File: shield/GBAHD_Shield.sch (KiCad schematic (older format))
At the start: 17 parts, among them J1 Conn_01x40, J2 Conn_02x08_Top_Bottom, J3 Conn_01x16, J4 Conn_02x10_Top_Bottom, J5 Conn_01x05, J6 Conn_02x03_Odd_Even, J7 Conn_01x01, SW1 SW_Push, U1 SNES_7PIN, U2 ATmega328P-AU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

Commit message: Version 2 initial commit.
- Changed board layout
- Changed breakout board pin order
- Changed FFC connectors
- Added connectors for 32 pin and 34 pin
- Changed SNES connector to Classic connector.
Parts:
- removed J5: Conn_01x05, OFFSET:Pads_01x05, symbol Connector_Generic:Conn_01x05
- removed J7: Conn_01x01, OFFSET:SOLDER_PAD, symbol Connector_Generic:Conn_01x01
- removed SJ1: SOLDER_JUMPER, Jumper:SolderJumper-2_P1.3mm_Open_RoundedPad1.0x1.5mm, symbol keyboard_parts:SOLDER_JUMPER
- removed U1: SNES_7PIN, OFFSET:SNES_7PIN, symbol Raizu:SNES_7PIN
- removed U3: WAS3157B, OFFSET:SOT-363, symbol Raizu:WAS3157B
- added J5: Conn_01x34, Raizu:JUSHUO_AFC07-S34FCC-00, symbol Connector_Generic:Conn_01x34
- added J7: Conn_01x32, Raizu:JUSHUO_AFC01-S32FCC-00, symbol Connector_Generic:Conn_01x32
- added P1: CONN_WII, Raizu_OFFSET:CONN_WII, symbol Raizu:CONN_WII
- added TP1: EX1, Raizu_OFFSET:SOLDER_PAD, symbol Connector:TestPoint
- added TP2: EX2, Raizu_OFFSET:SOLDER_PAD, symbol Connector:TestPoint
- added TP3: EX3, Raizu_OFFSET:SOLDER_PAD, symbol Connector:TestPoint
- added TP4: EX4, Raizu_OFFSET:SOLDER_PAD, symbol Connector:TestPoint
- J1: footprint OFFSET:JUSHUO_AFC07-S40FCC-00 -> Raizu:JUSHUO_AFC01-S40FCC-00
- J3: value Conn_01x16 -> Conn_01x20; footprint OFFSET:JUSHUO_AFC07-S16FCC-00 -> Raizu:JUSHUO_AFC01-S20FCC-00; symbol Connector_Generic:Conn_01x16 -> Connector_Generic:Conn_01x20
- SW1: footprint OFFSET:XKB-TS-1185EC-C-D-B -> Raizu_OFFSET:XKB-TS-1185EC-C-D-B
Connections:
- net labels added: GBA_RESET, JOY_DET, JOY_SCL, JOY_SDA
- net labels removed: GBA_POWER_SEL, SNS_CLK, SNS_DATA, SNS_LATCH
- wire segments 49 -> 59
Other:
- moved on the sheet: J2, J4

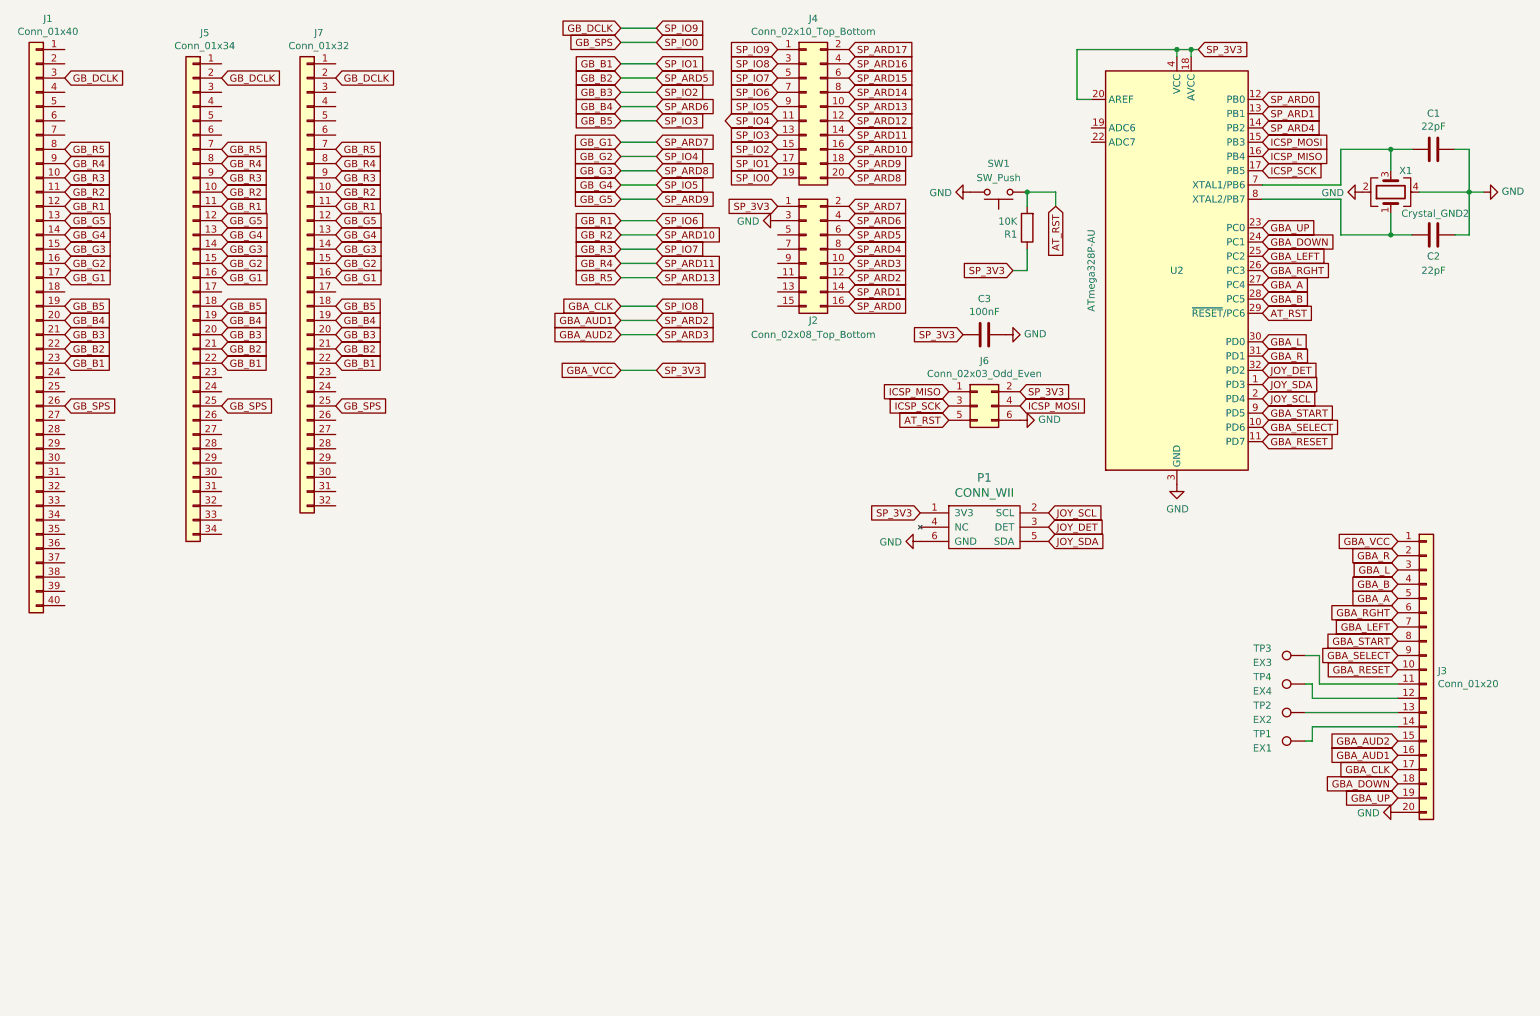
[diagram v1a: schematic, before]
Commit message: PCB changes and breakout board
- Added breakout to main board as a breakaway board.
- Added controller connector expansion for port relocation
- Tidying routing and other minimal changes
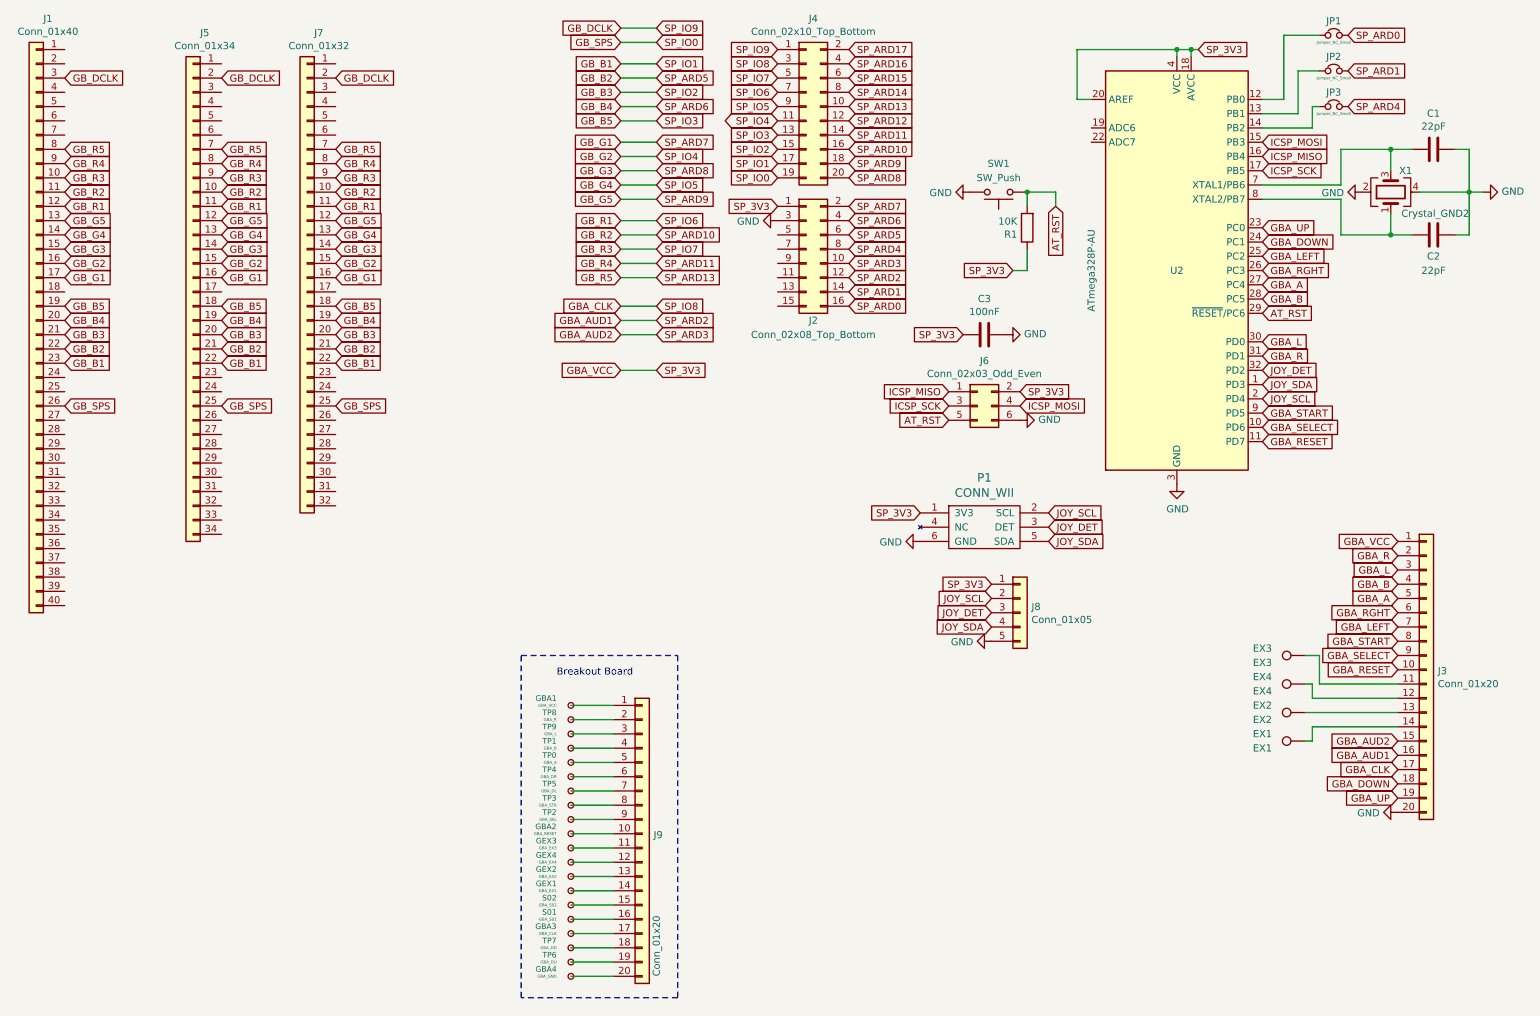
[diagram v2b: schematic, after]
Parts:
- added GBA1: GBA_VCC, Raizu_OFFSET:SOLDER_PAD, symbol Connector:TestPoint_Small
- added GBA2: GBA_RESET, Raizu_OFFSET:SOLDER_PAD, symbol Connector:TestPoint_Small
- added GBA3: GBA_CLK, Raizu_OFFSET:SOLDER_PAD, symbol Connector:TestPoint_Small
- added GBA4: GBA_GND, Raizu_OFFSET:SOLDER_PAD, symbol Connector:TestPoint_Small
- added GEX1: GBA_EX1, Raizu_OFFSET:SOLDER_PAD, symbol Connector:TestPoint_Small
- added GEX2: GBA_EX2, Raizu_OFFSET:SOLDER_PAD, symbol Connector:TestPoint_Small
- added GEX3: GBA_EX3, Raizu_OFFSET:SOLDER_PAD, symbol Connector:TestPoint_Small
- added GEX4: GBA_EX4, Raizu_OFFSET:SOLDER_PAD, symbol Connector:TestPoint_Small
- added J8: Conn_01x05, Connector_PinHeader_2.54mm:PinHeader_1x05_P2.54mm_Horizontal, symbol Connector_Generic:Conn_01x05
- added J9: Conn_01x20, Raizu:JUSHUO_AFC01-S20FCC-00, symbol Connector_Generic:Conn_01x20
- added JP1, JP2, JP3: Jumper_NC_Small, Jumper:SolderJumper-2_P1.3mm_Bridged_RoundedPad1.0x1.5mm, symbol Device:Jumper_NC_Small
- added S01: GBA_S01, Raizu_OFFSET:SOLDER_PAD, symbol Connector:TestPoint_Small
- added S02: GBA_S02, Raizu_OFFSET:SOLDER_PAD, symbol Connector:TestPoint_Small
- added TP0: GBA_A, Raizu_OFFSET:SOLDER_PAD, symbol Connector:TestPoint_Small
- added TP1: GBA_B, Raizu_OFFSET:SOLDER_PAD, symbol Connector:TestPoint_Small
- added TP2: GBA_SEL, Raizu_OFFSET:SOLDER_PAD, symbol Connector:TestPoint_Small
- added TP3: GBA_STR, Raizu_OFFSET:SOLDER_PAD, symbol Connector:TestPoint_Small
- added TP4: GBA_DR, Raizu_OFFSET:SOLDER_PAD, symbol Connector:TestPoint_Small
- added TP5: GBA_DL, Raizu_OFFSET:SOLDER_PAD, symbol Connector:TestPoint_Small
- added TP6: GBA_DU, Raizu_OFFSET:SOLDER_PAD, symbol Connector:TestPoint_Small
- added TP7: GBA_DD, Raizu_OFFSET:SOLDER_PAD, symbol Connector:TestPoint_Small
- added TP8: GBA_R, Raizu_OFFSET:SOLDER_PAD, symbol Connector:TestPoint_Small
- added TP9: GBA_L, Raizu_OFFSET:SOLDER_PAD, symbol Connector:TestPoint_Small
- renumbered TP1 to EX1, TP2 to EX2, TP3 to EX3, TP4 to EX4
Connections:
- net GBA_VCC: now also J8.1 (Pin_1)
- net GND: now also J8.5 (Pin_5)
- net JOY_DET: now also J8.3 (Pin_3)
- net JOY_SCL: now also J8.2 (Pin_2)
- net JOY_SDA: now also J8.4 (Pin_4)
- net SP_ARD0: now also JP1.2; no longer U2.12 (PB0)
- net SP_ARD1: now also JP2.2; no longer U2.13 (PB1)
- net SP_ARD4: now also JP3.2; no longer U2.14 (PB2)
- new net: JP1.1, U2.12 (PB0)
- new net: JP2.1, U2.13 (PB1)
- new net: JP3.1, U2.14 (PB2)
- new net: GBA1.1, J9.1 (Pin_1)
- new net: GBA2.1, J9.10 (Pin_10)
- new net: GEX3.1, J9.11 (Pin_11)
- new net: GEX4.1, J9.12 (Pin_12)
- new net: GEX2.1, J9.13 (Pin_13)
- new net: GEX1.1, J9.14 (Pin_14)
- new net: J9.15 (Pin_15), S02.1
- new net: J9.16 (Pin_16), S01.1
- new net: GBA3.1, J9.17 (Pin_17)
- new net: J9.18 (Pin_18), TP7.1
- new net: J9.19 (Pin_19), TP6.1
- new net: J9.2 (Pin_2), TP8.1
- new net: GBA4.1, J9.20 (Pin_20)
- new net: J9.3 (Pin_3), TP9.1
- new net: J9.4 (Pin_4), TP1.1
- new net: J9.5 (Pin_5), TP0.1
- new net: J9.6 (Pin_6), TP4.1
- new net: J9.7 (Pin_7), TP5.1
- new net: J9.8 (Pin_8), TP3.1
- new net: J9.9 (Pin_9), TP2.1
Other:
- note added: "Breakout Board"

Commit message: PCB design work
- Added extension board (controller, LED and power switch)
- Panelized board
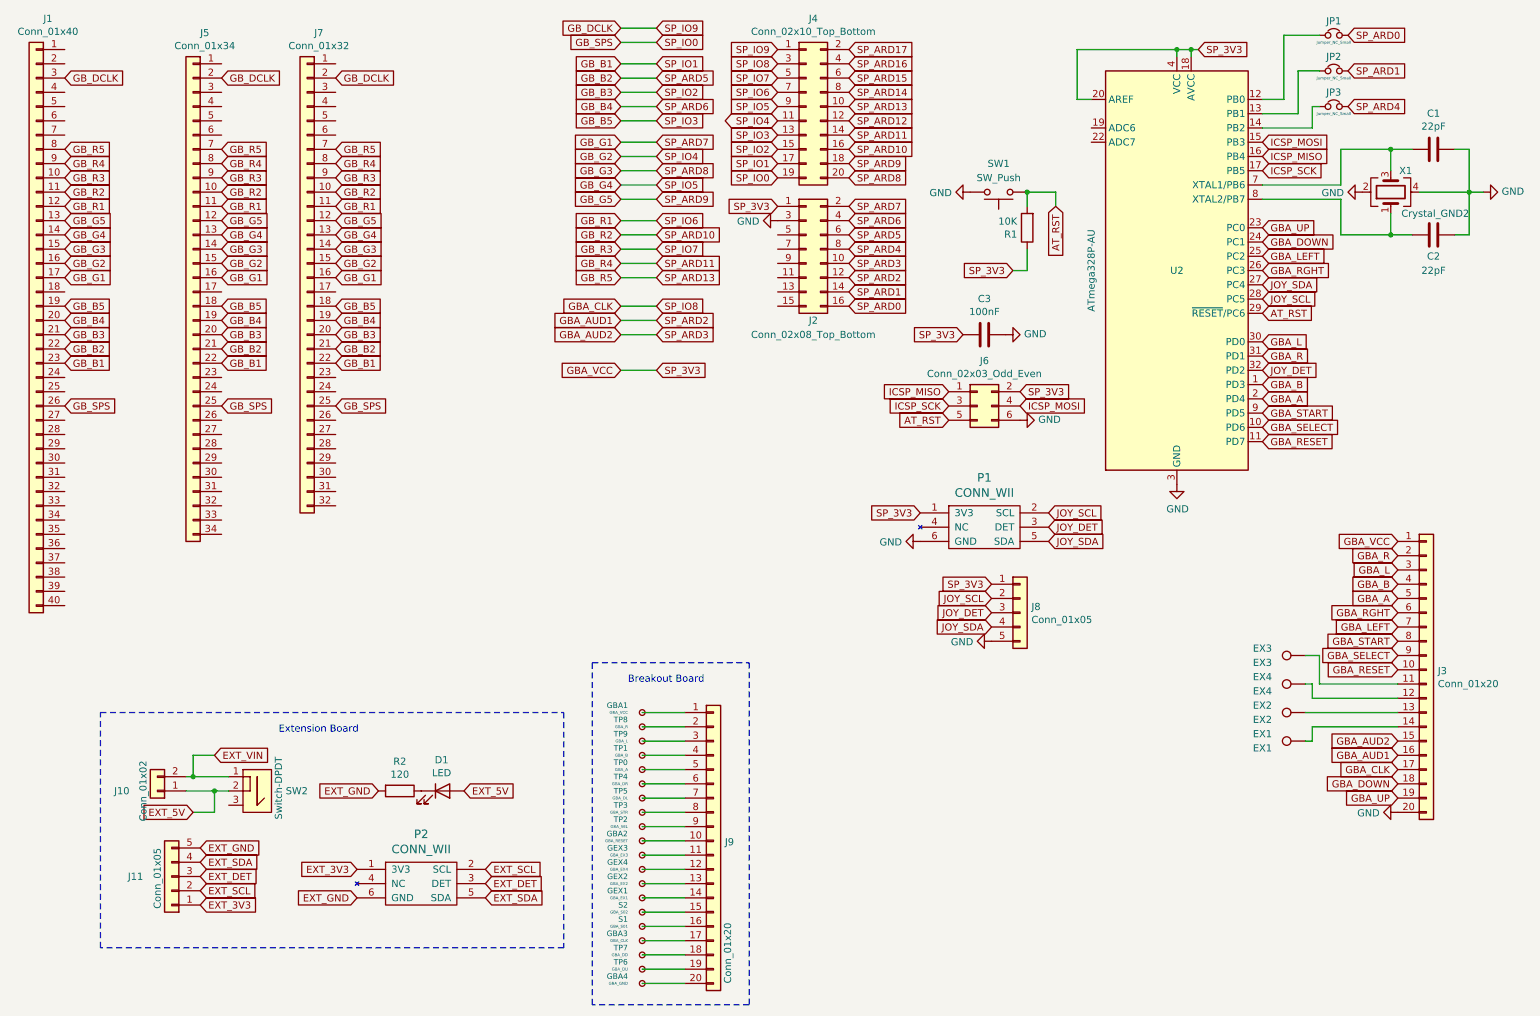
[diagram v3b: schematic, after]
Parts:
- added D1: LED, LED_THT:LED_D5.0mm_FlatTop, symbol Device:LED
- added J10: Conn_01x02, Connector_PinHeader_2.54mm:PinHeader_1x02_P2.54mm_Horizontal, symbol Connector_Generic:Conn_01x02
- added J11: Conn_01x05, Connector_PinHeader_2.54mm:PinHeader_1x05_P2.54mm_Horizontal, symbol Connector_Generic:Conn_01x05
- added P2: CONN_WII, Raizu_OFFSET:CONN_WII, symbol Raizu:CONN_WII
- added R2: 120, Resistor_SMD:R_0805_2012Metric_Pad1.20x1.40mm_HandSolder, symbol Device:R
- added SW2: Switch-DPDT, Raizu_OFFSET:XKB_XKB5858-Z-C, symbol Raizu:Switch-DPDT
- renumbered S01 to S1, S02 to S2
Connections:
- net GBA_A: now also U2.2 (PD4); no longer U2.27 (PC4)
- net GBA_B: now also U2.1 (PD3); no longer U2.28 (PC5)
- net JOY_SCL: now also U2.28 (PC5); no longer U2.2 (PD4)
- net JOY_SDA: now also U2.27 (PC4); no longer U2.1 (PD3)
- new net: D1.1 (K), R2.1
- new net EXT_3V3: J11.1 (Pin_1), P2.1 (3V3)
- new net EXT_5V: D1.2 (A), J10.1 (Pin_1), SW2.2
- new net EXT_DET: J11.3 (Pin_3), P2.3 (DET)
- new net EXT_GND: J11.5 (Pin_5), P2.6 (GND), R2.2
- new net EXT_SCL: J11.2 (Pin_2), P2.2 (SCL)
- new net EXT_SDA: J11.4 (Pin_4), P2.5 (SDA)
- new net EXT_VIN: J10.2 (Pin_2), SW2.1
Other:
- note added: "Extension Board"
- moved on the sheet: GBA1, GBA2, GBA3, GBA4, GEX1, GEX2, GEX3, GEX4, J9, S1, S2, TP0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
